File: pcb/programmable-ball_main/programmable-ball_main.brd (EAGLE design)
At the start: 29 x 29 mm, 19 parts, among them J1 12402012E212A, P1 S2B-ZR-SM4A-TF, Q1 DMG2305UX-13, SW1 CAS-120CAS-120B1, U1 MDBT50Q-1MV2, U2 AP2112K-3.3TRG1, Y1 FC-135_32.7680KA-A0

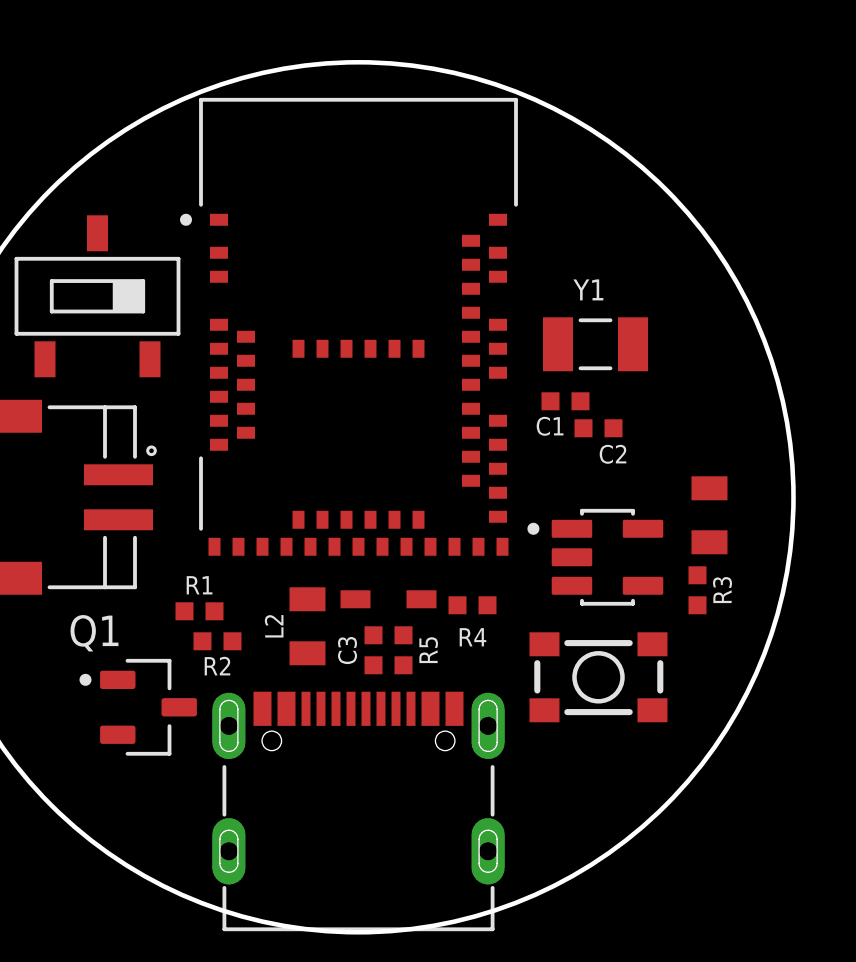
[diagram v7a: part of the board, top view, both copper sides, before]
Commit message: 配置を微修正
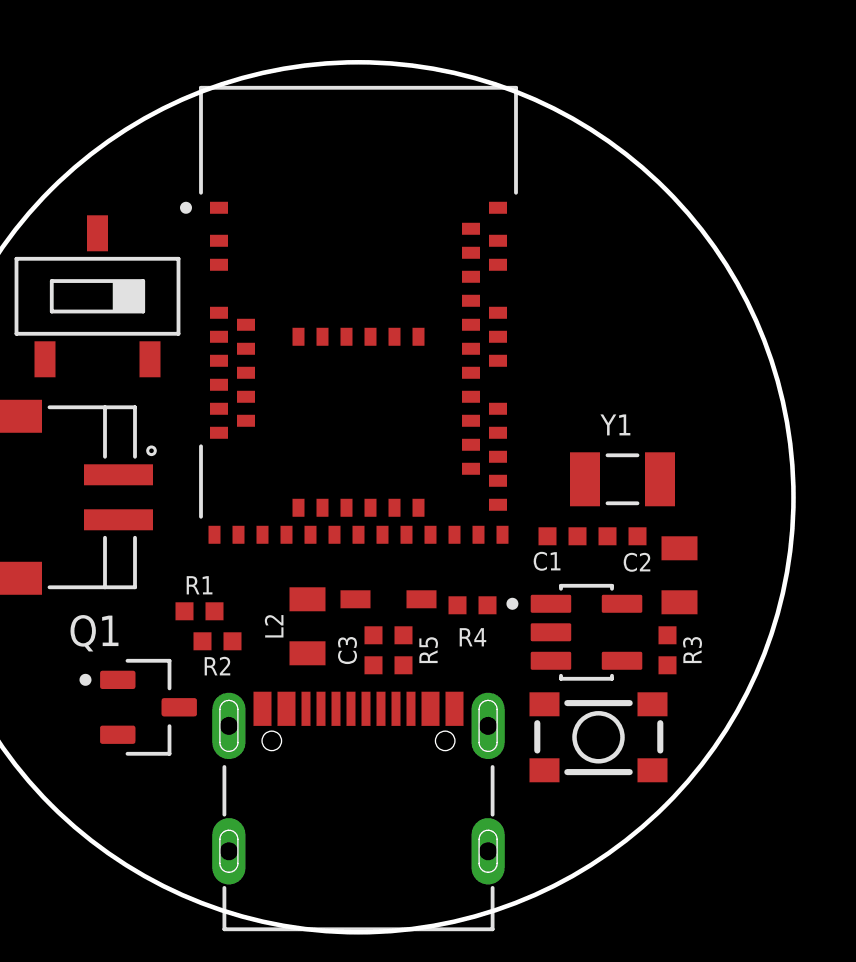
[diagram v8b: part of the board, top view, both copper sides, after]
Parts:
- moved Y1 4.59 mm to (23.8, 15.6)
- moved C1 4.50 mm to (21.8, 13.7)
- moved C2 3.69 mm to (23.8, 13.7)
- moved U2 2.60 mm to (22.6, 10.5)
- moved L1 2.24 mm to (25.7, 12.4)
- moved R3 2.24 mm to (25.3, 9.90)
- moved S1 2.00 mm to (23.0, 7.00)
- moved U1 0.40 mm to (15.0, 20.9)
